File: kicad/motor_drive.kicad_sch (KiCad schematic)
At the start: 7 parts, among them U2 DRV8452DDWR

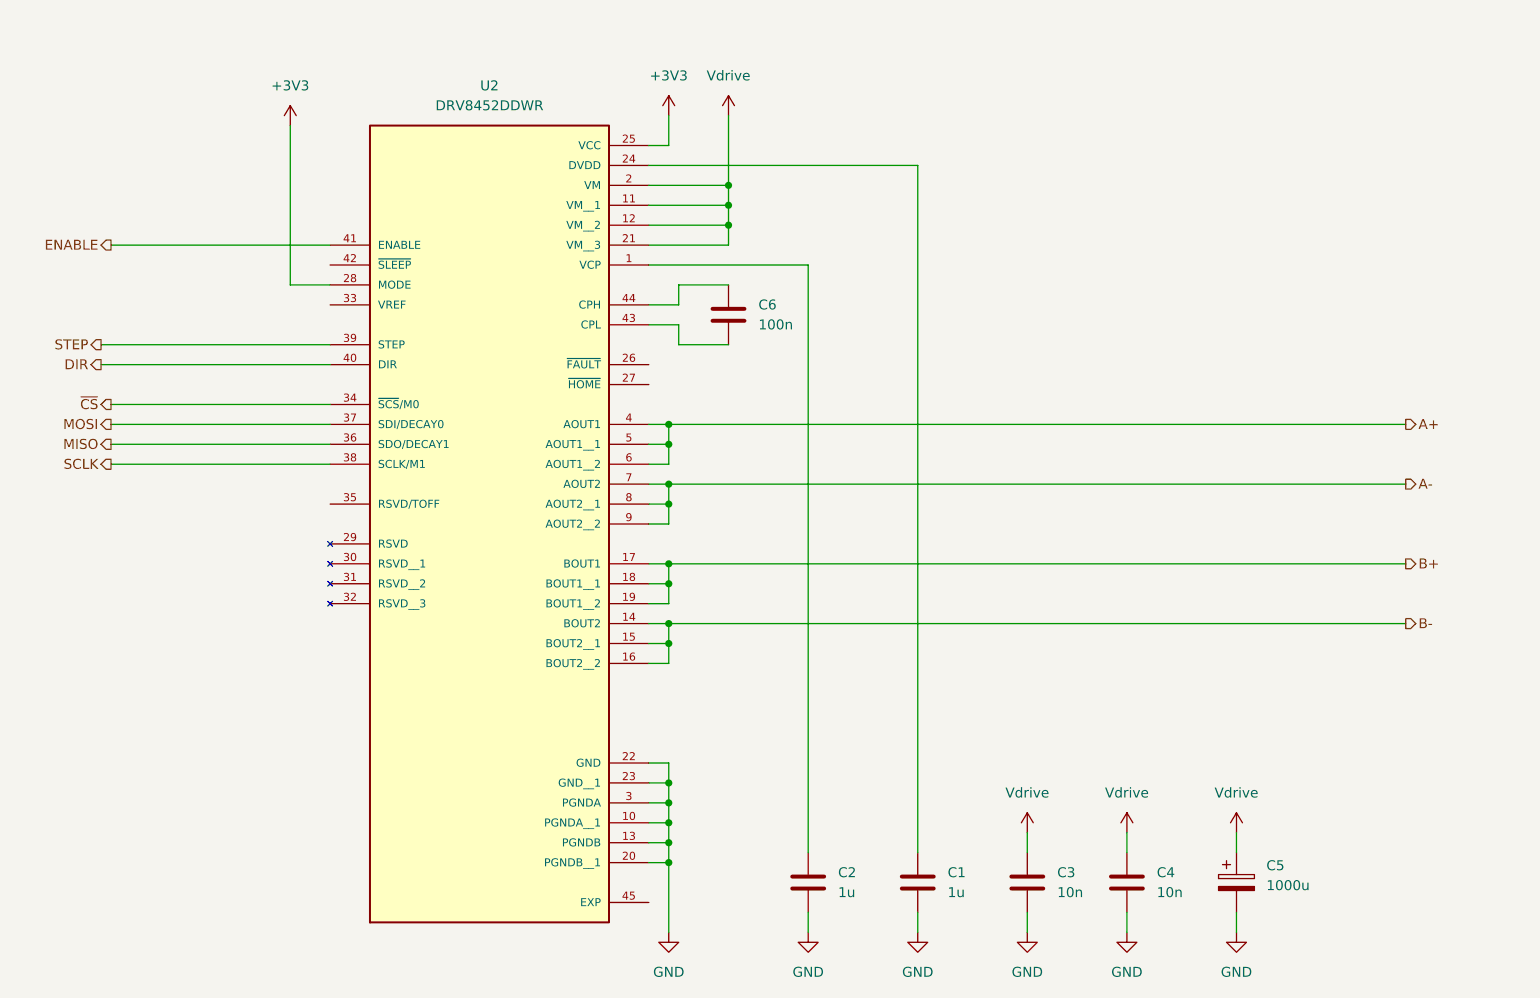
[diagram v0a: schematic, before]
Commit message: Completed the schematic. All components have Digikey part numbers and footprints. The power supply sheet still requires some work.
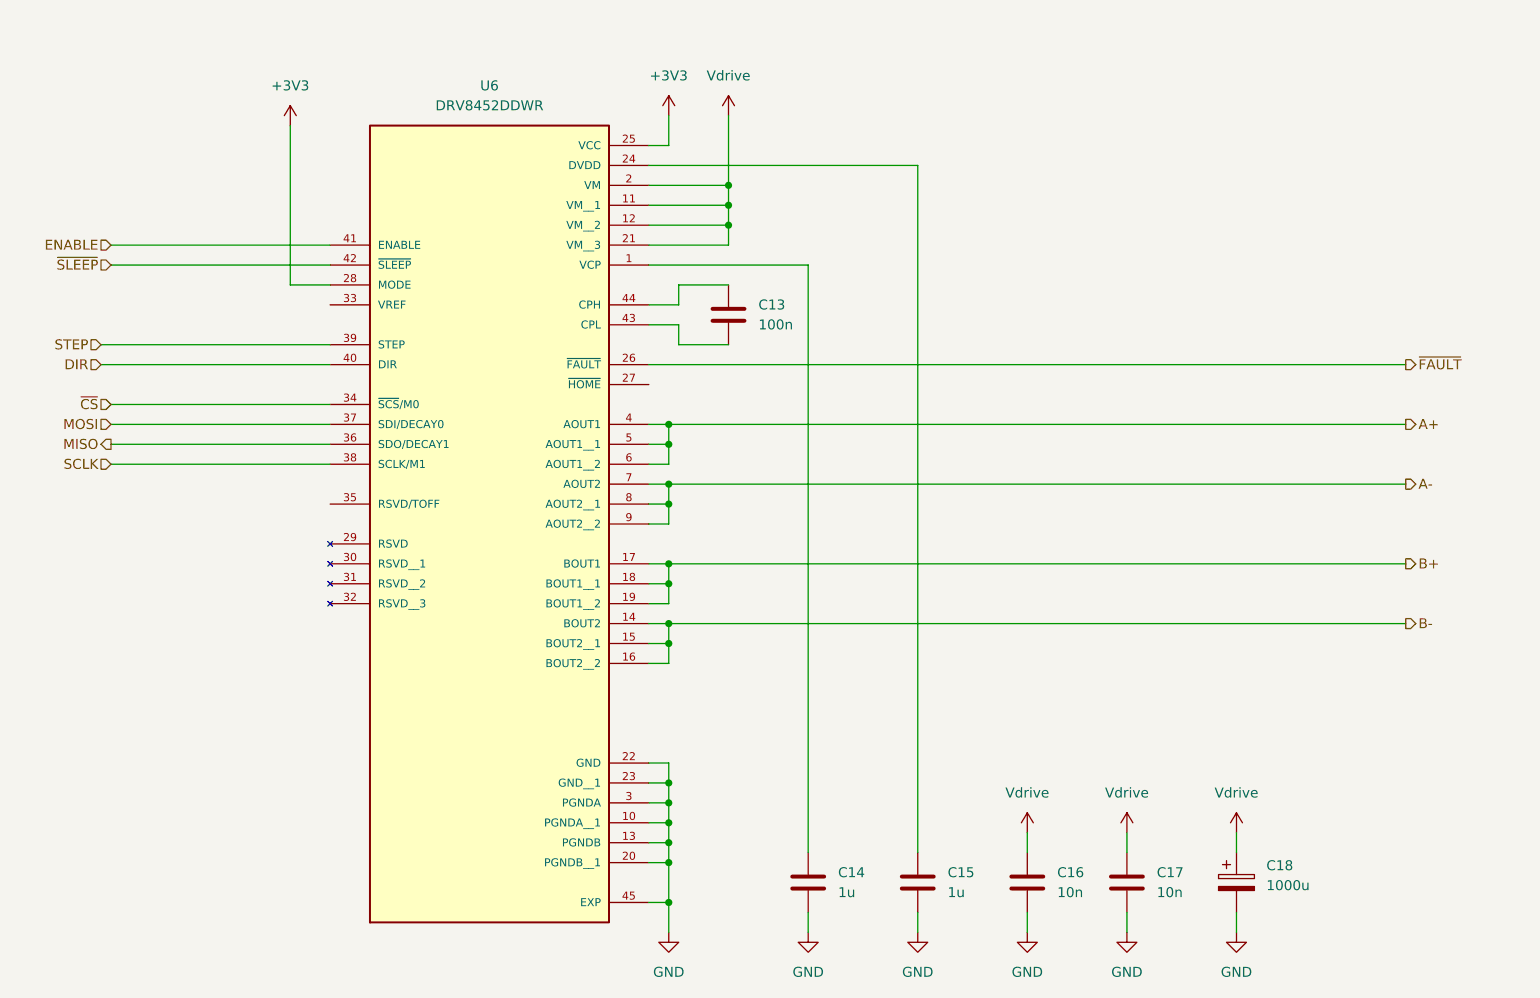
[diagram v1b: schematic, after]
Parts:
- C13: renamed from C6; footprint (none) -> Capacitor_SMD:C_0603_1608Metric; Dielectric (none) -> X7R; MF (none) -> Murata; MP (none) -> GRM188R72A104KA35D; Supplier (none) -> Digi-Key; SupplierPN (none) -> 490-3890-1-ND; Voltage (none) -> 100V; Voltage rating 63V -> (none)
- C14: renamed from C2; footprint (none) -> Capacitor_SMD:C_0805_2012Metric; Dielectric (none) -> X7R; MF (none) -> Murata; MP (none) -> GRM21BR72A105KE01L; Supplier (none) -> Digi-Key; SupplierPN (none) -> 490-5526-1-ND; Voltage (none) -> 100V; Voltage rating 16V -> (none)
- C15: renamed from C1; footprint (none) -> Capacitor_SMD:C_0805_2012Metric; Dielectric (none) -> X7R; MF (none) -> Murata; MP (none) -> GRM21BR72A105KE01L; Supplier (none) -> Digi-Key; SupplierPN (none) -> 490-5526-1-ND; Voltage (none) -> 100V; Voltage rating 10V -> (none)
- C16: renamed from C3; footprint (none) -> Capacitor_SMD:C_0603_1608Metric; Dielectric (none) -> X7R; MF (none) -> Murata; MP (none) -> GRM188R71H103KA01D; Supplier (none) -> Digi-Key; SupplierPN (none) -> 490-6377-1-ND; Voltage (none) -> 50V; Voltage rating 63V -> (none)
- C17: renamed from C4; footprint (none) -> Capacitor_SMD:C_0603_1608Metric; Dielectric (none) -> X7R; MF (none) -> Murata; MP (none) -> GRM188R71H103KA01D; Supplier (none) -> Digi-Key; SupplierPN (none) -> 490-6377-1-ND; Voltage (none) -> 50V; Voltage rating 63V -> (none)
- C18: renamed from C5; footprint (none) -> Capacitor_THT:CP_Radial_D12.5mm_P5.00mm; Dielectric (none) -> Electrolytic; MF (none) -> Panasonic; MP (none) -> EEU-FR1J102; Supplier (none) -> Digi-Key; SupplierPN (none) -> P12418-ND; Voltage (none) -> 63V; Voltage rating 63V -> (none)
- U6: renamed from U2; MF (none) -> TI; MP (none) -> DRV8452DDWR; Supplier (none) -> Digi-Key; SupplierPN (none) -> 296-DRV8452DDWRCT-ND
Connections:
- net GND: now also U6.45 (EXP)
- net ~{FAULT}: now reaches U6.26 (~{FAULT})
- net ~{SLEEP}: now reaches U6.42 (~{SLEEP})
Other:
- company: (none) -> NX Solutions
- title: (none) -> TV slider

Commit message: Updated footprints and step models. Placed on PCB, but not yet positioned in final location.
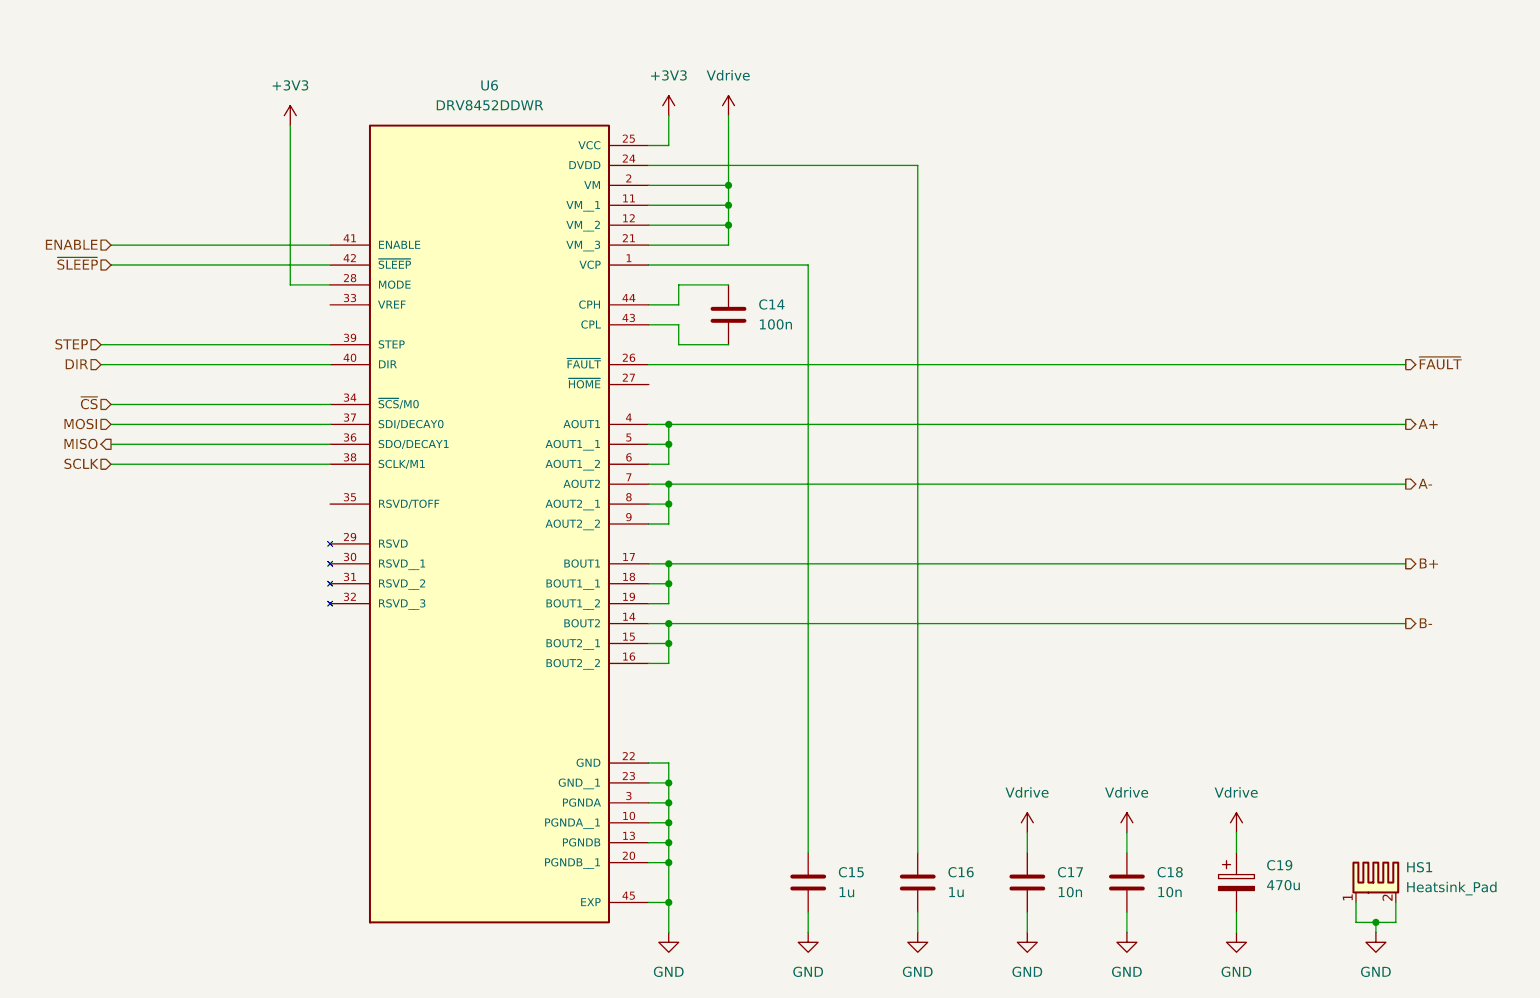
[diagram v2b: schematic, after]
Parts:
- added HS1: Heatsink_Pad, local_library:ATS-TI1OP-519-C1-R3, symbol Mechanical:Heatsink_Pad_2Pin
- C14: renamed from C13; SupplierPN 490-3890-1-ND -> 490-3285-1-ND
- C15: renamed from C14; Dielectric X7R -> X7S; MP GRM21BR72A105KE01L -> GRM21BC72A105KE01L; SupplierPN 490-5526-1-ND -> 490-14464-1-ND
- C16: renamed from C15; Dielectric X7R -> X7S; MP GRM21BR72A105KE01L -> GRM21BC72A105KE01L; SupplierPN 490-5526-1-ND -> 490-14464-1-ND
- C17: renamed from C16; MP GRM188R71H103KA01D -> GRM188R72A103KA01D; SupplierPN 490-6377-1-ND -> 490-GRM188R72A103KA01DCT-ND; Voltage 50V -> 100V
- C18: renamed from C17; MP GRM188R71H103KA01D -> GRM188R72A103KA01D; SupplierPN 490-6377-1-ND -> 490-GRM188R72A103KA01DCT-ND; Voltage 50V -> 100V
- C19: renamed from C18; value 1000u -> 470u; footprint Capacitor_THT:CP_Radial_D12.5mm_P5.00mm -> local_library:CP_Radial_D18.0mm_P7.50mm_Horizontal; MF Panasonic -> Kemet; MP EEU-FR1J102 -> EST477M100AN5AA; SupplierPN P12418-ND -> 399-15749-ND; Voltage 63V -> 100V
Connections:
- net GND: now also HS1.1, HS1.2

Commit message: Updated all schematic pages except the power supply. Did the initial component placement.
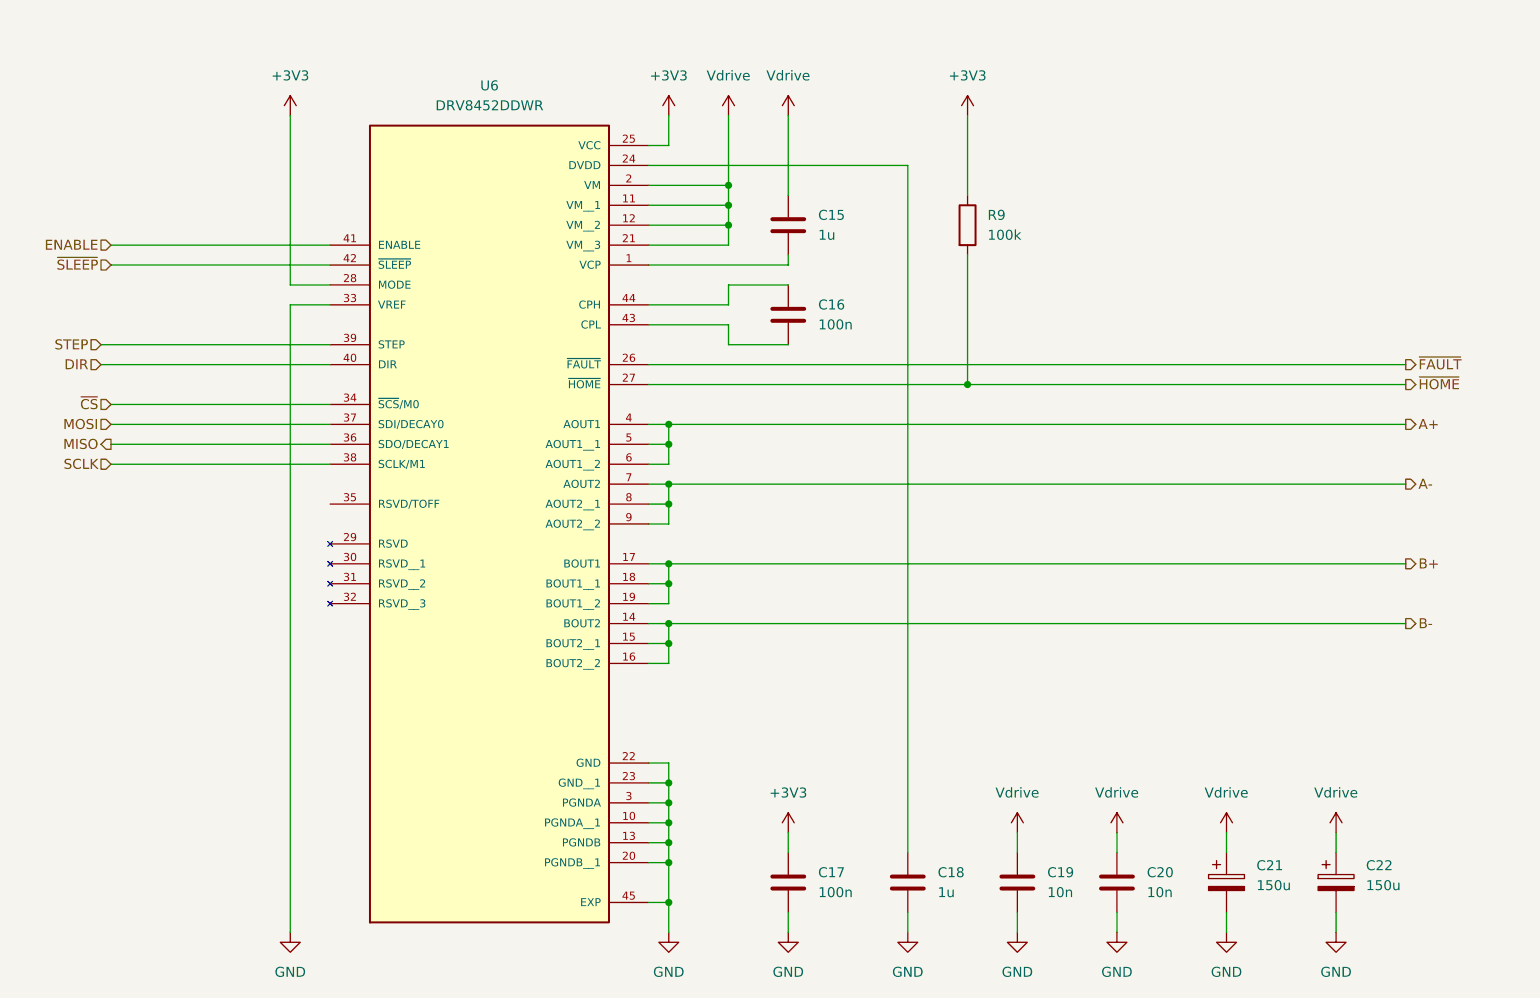
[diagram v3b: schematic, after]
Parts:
- removed HS1: Heatsink_Pad, local_library:ATS-TI1OP-519-C1-R3, symbol Mechanical:Heatsink_Pad_2Pin
- added C17: 100n, Capacitor_SMD:C_0603_1608Metric, symbol Device:C
- added C22: 150u, Capacitor_SMD:CP_Elec_10x12.5, symbol Device:C_Polarized
- added R9: 100k, Resistor_SMD:R_0603_1608Metric, symbol Device:R
- C21: renamed from C19; value 470u -> 150u; footprint local_library:CP_Radial_D18.0mm_P7.50mm_Horizontal -> Capacitor_SMD:CP_Elec_10x12.5; MP EST477M100AN5AA -> A768MS157M1HLAE024; SupplierPN 399-15749-ND -> 399-A768MS157M1HLAE024TR-ND; Voltage 100V -> 50V
- renumbered C14 to C16, C16 to C18, C17 to C19, C18 to C20
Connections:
- net +3V3: now also C17.1, R9.1
- net GND: now also U6.33 (VREF), C17.2, C22.2; no longer C15.2
- net Vdrive: now also C15.1, C22.1
- net at U6.1 (VCP): now also C15.2; no longer C15.1
- net ~{HOME}: now reaches U6.27 (~{HOME})
- net ~{HOME}: now also R9.2
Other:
- moved on the sheet: C15, C16, C18, C19, C20, C21
